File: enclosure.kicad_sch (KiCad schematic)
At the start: 17 parts, among them J101 Conn_01x06_Socket, J102 Conn_01x02_Socket

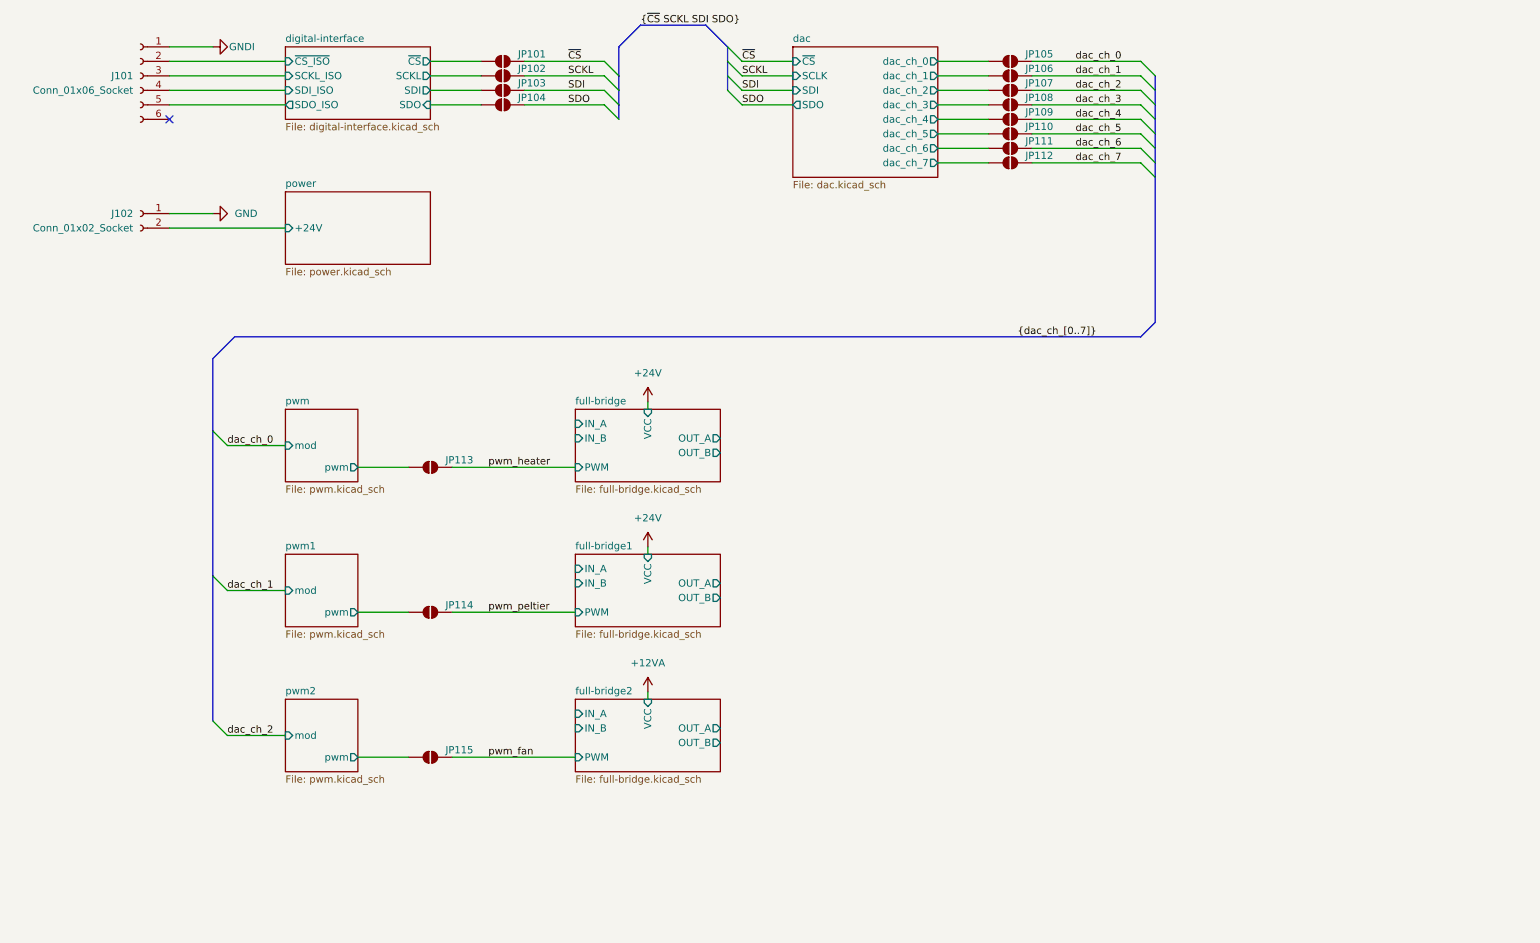
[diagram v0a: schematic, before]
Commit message: add enclosure output connectors
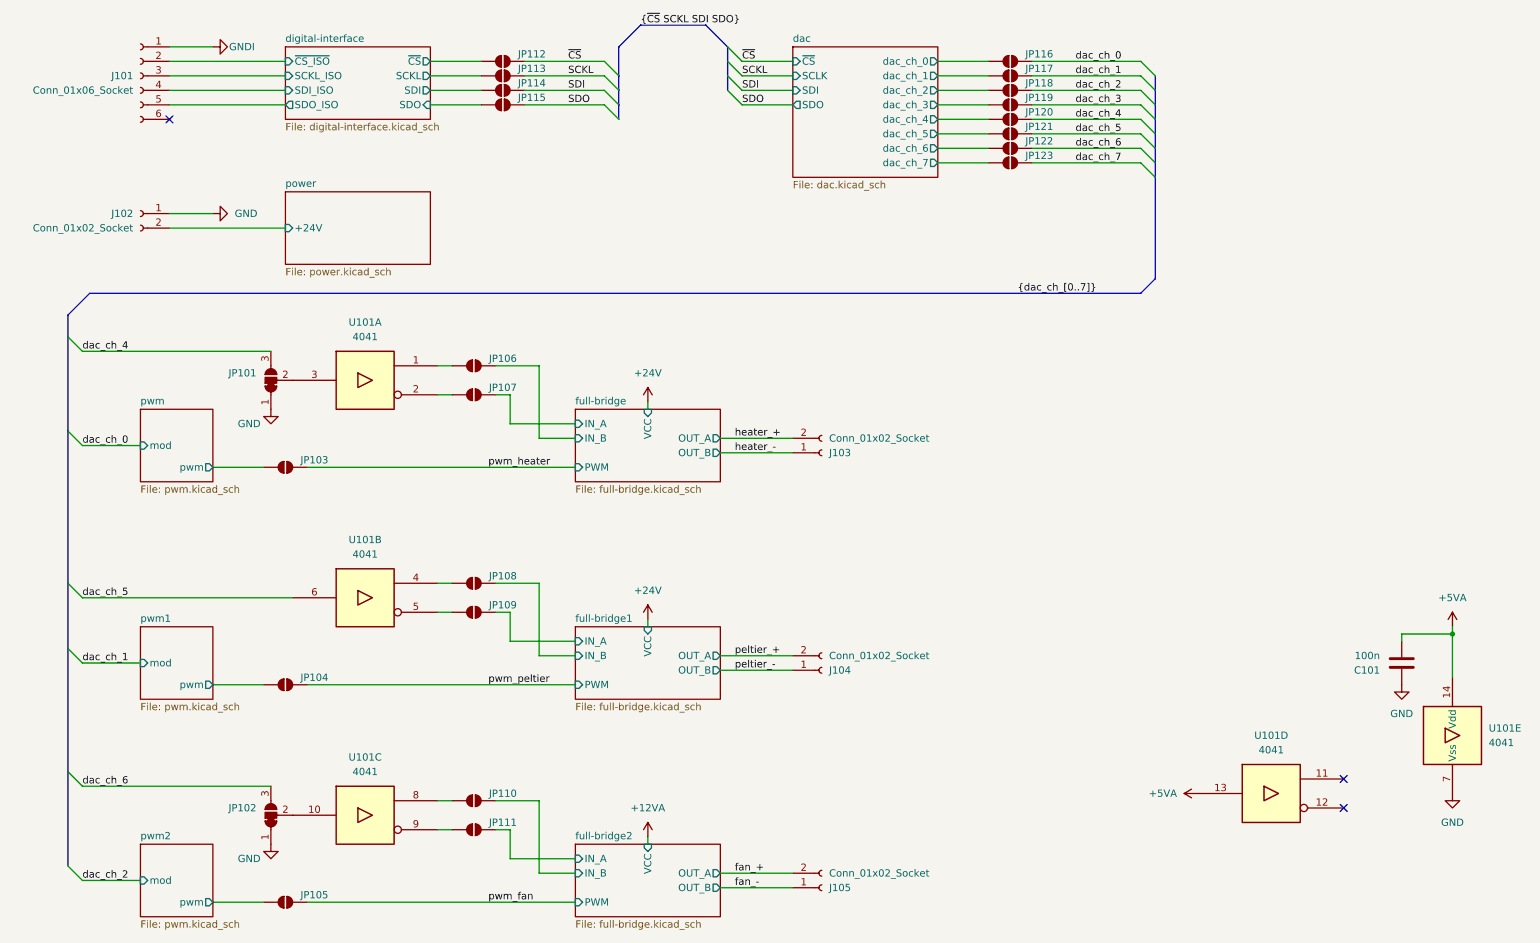
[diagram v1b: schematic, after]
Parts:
- added C101: 100n, pss:C_0805_2012Metric_Pad1.18x1.45mm_HandSolder, symbol enclosure:C
- added J103, J104, J105: Conn_01x02_Socket, pss:PhoenixContact_TDPT_2,5_2-SP-5,08_1x02_P5.08mm_Horizontal, symbol enclosure:Conn_01x02_Socket
- added JP101, JP102: SolderJumper_3_Bridged12, pss:SolderJumper-3_P1.3mm_Bridged12-Soldermask-Paste_RoundedPad1.0x1.5mm, symbol enclosure:SolderJumper_3_Bridged12
- added JP106, JP107, JP108, JP109, JP110, JP111: SolderJumper_2_Open, pss:SolderJumper-2_P1.3mm_Open_RoundedPad1.0x1.5mm, symbol enclosure:SolderJumper_2_Open
- added U101: 4041, pss:SOIC-14_3.9x8.7mm_P1.27mm, symbol enclosure:4041
- renumbered JP113 to JP103, JP114 to JP104, JP115 to JP105, JP101 to JP112, JP102 to JP113, JP103 to JP114, JP104 to JP115, JP105 to JP116, JP106 to JP117, JP107 to JP118, JP108 to JP119, JP109 to JP120, JP110 to JP121, JP111 to JP122, JP112 to JP123
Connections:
- net GND: now also C101.1, JP101.1 (A), JP102.1 (A), U101.7 (Vss)
- net dac_ch_4: now also JP101.3 (B)
- net dac_ch_5: now also U101.6
- net dac_ch_6: now also JP102.3 (B)
- net full-bridge/IN_A: now also JP107.2 (B)
- net full-bridge/IN_B: now also JP106.2 (B)
- net full-bridge1/IN_A: now also JP109.2 (B)
- net full-bridge1/IN_B: now also JP108.2 (B)
- net full-bridge2/IN_A: now also JP111.2 (B)
- net full-bridge2/IN_B: now also JP110.2 (B)
- new net: JP109.1 (A), U101.5
- new net: JP102.2 (C), U101.10
- new net: JP110.1 (A), U101.8
- new net: JP111.1 (A), U101.9
- new net: JP108.1 (A), U101.4
- new net: JP106.1 (A), U101.1
- new net: JP107.1 (A), U101.2
- new net: JP101.2 (C), U101.3
- new net +5VA: C101.2, U101.13, U101.14 (Vdd)
- new net fan_+: J105.2 (Pin_2)
- new net fan_-: J105.1 (Pin_1)
- new net heater_+: J103.2 (Pin_2)
- new net heater_-: J103.1 (Pin_1)
- new net peltier_+: J104.2 (Pin_2)
- new net peltier_-: J104.1 (Pin_1)
- no-connect marks 1 -> 3
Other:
- moved on the sheet: JP103, JP104, JP105

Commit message: update datasheets and footprint references
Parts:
- C101: footprint pss:C_0805_2012Metric_Pad1.18x1.45mm_HandSolder -> enclosure:C_0805_2012Metric_Pad1.18x1.45mm_HandSolder
- J101: footprint pss:PhoenixContact_TDPT_2,5_6-SP-5,08_1x06_P5.08mm_Horizontal -> enclosure:PhoenixContact_TDPT_2,5_6-SP-5,08_1x06_P5.08mm_Horizontal
- J102, J103, J104, J105: footprint pss:PhoenixContact_TDPT_2,5_2-SP-5,08_1x02_P5.08mm_Horizontal -> enclosure:PhoenixContact_TDPT_2,5_2-SP-5,08_1x02_P5.08mm_Horizontal
- JP101, JP102: footprint pss:SolderJumper-3_P1.3mm_Bridged12-Soldermask-Paste_RoundedPad1.0x1.5mm -> enclosure:SolderJumper-3_P1.3mm_Bridged12-Soldermask-Paste_RoundedPad1.0x1.5mm
- JP103, JP104, JP105, JP106, JP107, JP108, JP109, JP110, JP111, JP112, JP113, JP114, JP115, JP116, JP117, JP118, JP119, JP120, JP121, JP122, JP123: footprint pss:SolderJumper-2_P1.3mm_Open_RoundedPad1.0x1.5mm -> enclosure:SolderJumper-2_P1.3mm_Open_RoundedPad1.0x1.5mm
- U101: footprint pss:SOIC-14_3.9x8.7mm_P1.27mm -> enclosure:SOIC-14_3.9x8.7mm_P1.27mm
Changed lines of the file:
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@@
 			)
 		)
-		(property "Footprint" "pss:SolderJumper-2_P1.3mm_Open_RoundedPad1.0x1.5mm"
+		(property "Footprint" "enclosure:SolderJumper-2_P1.3mm_Open_RoundedPad1.0x1.5mm"
 			(at 101.6 30.48 0)
 			(effects
@@
 			)
 		)
-		(property "Footprint" "pss:SolderJumper-2_P1.3mm_Open_RoundedPad1.0x1.5mm"
+		(property "Footprint" "enclosure:SolderJumper-2_P1.3mm_Open_RoundedPad1.0x1.5mm"
 			(at 96.52 124.46 0)
 			(effects
@@
 			)
 		)
-		(property "Footprint" "pss:PhoenixContact_TDPT_2,5_2-SP-5,08_1x02_P5.08mm_Horizontal"
+		(property "Footprint" "enclosure:PhoenixContact_TDPT_2,5_2-SP-5,08_1x02_P5.08mm_Horizontal"
 			(at 38.1 54.61 0)
 			(effects
@@
 			)
 		)
-		(property "Footprint" "pss:SolderJumper-2_P1.3mm_Open_RoundedPad1.0x1.5mm"
+		(property "Footprint" "enclosure:SolderJumper-2_P1.3mm_Open_RoundedPad1.0x1.5mm"
 			(at 190.5 27.94 0)
 			(effects
@@
 			)
 		)
-		(property "Footprint" "pss:PhoenixContact_TDPT_2,5_6-SP-5,08_1x06_P5.08mm_Horizontal"
+		(property "Footprint" "enclosure:PhoenixContact_TDPT_2,5_6-SP-5,08_1x06_P5.08mm_Horizontal"
 			(at 38.1 30.48 0)
 			(effects
@@
 			)
 		)
-		(property "Footprint" "pss:SolderJumper-2_P1.3mm_Open_RoundedPad1.0x1.5mm"
+		(property "Footprint" "enclosure:SolderJumper-2_P1.3mm_Open_RoundedPad1.0x1.5mm"
 			(at 190.5 45.72 0)
 			(effects
@@
 			)
 		)
-		(property "Footprint" "pss:SolderJumper-2_P1.3mm_Open_RoundedPad1.0x1.5mm"
+		(property "Footprint" "enclosure:SolderJumper-2_P1.3mm_Open_RoundedPad1.0x1.5mm"
 			(at 190.5 38.1 0)
 			(effects
@@
 			)
 		)
-		(property "Footprint" "pss:PhoenixContact_TDPT_2,5_2-SP-5,08_1x02_P5.08mm_Horizontal"
+		(property "Footprint" "enclosure:PhoenixContact_TDPT_2,5_2-SP-5,08_1x02_P5.08mm_Horizontal"
 			(at 157.48 172.72 0)
 			(effects
@@
 			)
 		)
-		(property "Footprint" "pss:SolderJumper-2_P1.3mm_Open_RoundedPad1.0x1.5mm"
+		(property "Footprint" "enclosure:SolderJumper-2_P1.3mm_Open_RoundedPad1.0x1.5mm"
 			(at 190.5 40.64 0)
 			(effects
@@
 			)
 		)
-		(property "Footprint" "pss:PhoenixContact_TDPT_2,5_2-SP-5,08_1x02_P5.08mm_Horizontal"
+		(property "Footprint" "enclosure:PhoenixContact_TDPT_2,5_2-SP-5,08_1x02_P5.08mm_Horizontal"
 			(at 157.48 134.62 0)
 			(effects
@@
 			)
 		)
-		(property "Footprint" "pss:SolderJumper-2_P1.3mm_Open_RoundedPad1.0x1.5mm"
+		(property "Footprint" "enclosure:SolderJumper-2_P1.3mm_Open_RoundedPad1.0x1.5mm"
 			(at 190.5 33.02 0)
 			(effects
@@
 			)
 		)
-		(property "Footprint" "pss:SOIC-14_3.9x8.7mm_P1.27mm"
+		(property "Footprint" "enclosure:SOIC-14_3.9x8.7mm_P1.27mm"
 			(at 77.47 160.02 0)
 			(effects
@@
 			)
 		)
-		(property "Footprint" "pss:SolderJumper-2_P1.3mm_Open_RoundedPad1.0x1.5mm"
+		(property "Footprint" "enclosure:SolderJumper-2_P1.3mm_Open_RoundedPad1.0x1.5mm"
 			(at 96.52 119.38 0)
 			(effects
@@
 			)
 		)
-		(property "Footprint" "pss:SolderJumper-3_P1.3mm_Bridged12-Soldermask-Paste_RoundedPad1.0x1.5mm"
+		(property "Footprint" "enclosure:SolderJumper-3_P1.3mm_Bridged12-Soldermask-Paste_RoundedPad1.0x1.5mm"
 			(at 60.96 160.02 0)
 			(effects
@@
 			)
 		)
-		(property "Footprint" "pss:C_0805_2012Metric_Pad1.18x1.45mm_HandSolder"
+		(property "Footprint" "enclosure:C_0805_2012Metric_Pad1.18x1.45mm_HandSolder"
 			(at 258.1148 129.54 0)
 			(effects
@@
 			)
 		)
-		(property "Footprint" "pss:SolderJumper-2_P1.3mm_Open_RoundedPad1.0x1.5mm"
+		(property "Footprint" "enclosure:SolderJumper-2_P1.3mm_Open_RoundedPad1.0x1.5mm"
 			(at 96.52 157.48 0)
 			(effects
@@
 			)
 		)
-		(property "Footprint" "pss:SolderJumper-2_P1.3mm_Open_RoundedPad1.0x1.5mm"
+		(property "Footprint" "enclosure:SolderJumper-2_P1.3mm_Open_RoundedPad1.0x1.5mm"
 			(at 101.6 35.56 0)
 			(effects
@@
 			)
 		)
-		(property "Footprint" "pss:PhoenixContact_TDPT_2,5_2-SP-5,08_1x02_P5.08mm_Horizontal"
+		(property "Footprint" "enclosure:PhoenixContact_TDPT_2,5_2-SP-5,08_1x02_P5.08mm_Horizontal"
 			(at 157.48 96.52 0)
 			(effects
@@
 			)
 		)
-		(property "Footprint" "pss:SolderJumper-2_P1.3mm_Open_RoundedPad1.0x1.5mm"
+		(property "Footprint" "enclosure:SolderJumper-2_P1.3mm_Open_RoundedPad1.0x1.5mm"
 			(at 63.5 175.26 0)
 			(effects
@@
 			)
 		)
-		(property "Footprint" "pss:SolderJumper-2_P1.3mm_Open_RoundedPad1.0x1.5mm"
+		(property "Footprint" "enclosure:SolderJumper-2_P1.3mm_Open_RoundedPad1.0x1.5mm"
 			(at 190.5 43.18 0)
 			(effects
@@
 			)
 		)
-		(property "Footprint" "pss:SolderJumper-2_P1.3mm_Open_RoundedPad1.0x1.5mm"
+		(property "Footprint" "enclosure:SolderJumper-2_P1.3mm_Open_RoundedPad1.0x1.5mm"
 			(at 101.6 27.94 0)
 			(effects
@@
 			)
 		)
-		(property "Footprint" "pss:SOIC-14_3.9x8.7mm_P1.27mm"
+		(property "Footprint" "enclosure:SOIC-14_3.9x8.7mm_P1.27mm"
 			(at 77.47 83.82 0)
 			(effects
@@
 			)
 		)
-		(property "Footprint" "pss:SolderJumper-2_P1.3mm_Open_RoundedPad1.0x1.5mm"
+		(property "Footprint" "enclosure:SolderJumper-2_P1.3mm_Open_RoundedPad1.0x1.5mm"
 			(at 96.52 81.28 0)
 			(effects
@@
 			)
 		)
-		(property "Footprint" "pss:SOIC-14_3.9x8.7mm_P1.27mm"
+		(property "Footprint" "enclosure:SOIC-14_3.9x8.7mm_P1.27mm"
 			(at 77.47 121.92 0)
 			(effects
@@
 			)
 		)
-		(property "Footprint" "pss:SolderJumper-2_P1.3mm_Open_RoundedPad1.0x1.5mm"
+		(property "Footprint" "enclosure:SolderJumper-2_P1.3mm_Open_RoundedPad1.0x1.5mm"
 			(at 190.5 35.56 0)
 			(effects
@@
 			)
 		)
-		(property "Footprint" "pss:SolderJumper-2_P1.3mm_Open_RoundedPad1.0x1.5mm"
+		(property "Footprint" "enclosure:SolderJumper-2_P1.3mm_Open_RoundedPad1.0x1.5mm"
 			(at 190.5 30.48 0)
 			(effects
@@
 			)
 		)
-		(property "Footprint" "pss:SOIC-14_3.9x8.7mm_P1.27mm"
+		(property "Footprint" "enclosure:SOIC-14_3.9x8.7mm_P1.27mm"
 			(at 267.97 146.05 0)
 			(effects
@@
 			)
 		)
-		(property "Footprint" "pss:SOIC-14_3.9x8.7mm_P1.27mm"
+		(property "Footprint" "enclosure:SOIC-14_3.9x8.7mm_P1.27mm"
 			(at 236.22 156.21 0)
 			(effects
@@
 			)
 		)
-		(property "Footprint" "pss:SolderJumper-2_P1.3mm_Open_RoundedPad1.0x1.5mm"
+		(property "Footprint" "enclosure:SolderJumper-2_P1.3mm_Open_RoundedPad1.0x1.5mm"
 			(at 63.5 99.06 0)
 			(effects
@@
 			)
 		)
-		(property "Footprint" "pss:SolderJumper-2_P1.3mm_Open_RoundedPad1.0x1.5mm"
+		(property "Footprint" "enclosure:SolderJumper-2_P1.3mm_Open_RoundedPad1.0x1.5mm"
 			(at 63.5 137.16 0)
 			(effects
@@
 			)
 		)
-		(property "Footprint" "pss:SolderJumper-2_P1.3mm_Open_RoundedPad1.0x1.5mm"
+		(property "Footprint" "enclosure:SolderJumper-2_P1.3mm_Open_RoundedPad1.0x1.5mm"
 			(at 101.6 33.02 0)
 			(effects
@@
 			)
 		)
-		(property "Footprint" "pss:SolderJumper-2_P1.3mm_Open_RoundedPad1.0x1.5mm"
+		(property "Footprint" "enclosure:SolderJumper-2_P1.3mm_Open_RoundedPad1.0x1.5mm"
 			(at 96.52 162.56 0)
 			(effects
@@
 			)
 		)
-		(property "Footprint" "pss:SolderJumper-3_P1.3mm_Bridged12-Soldermask-Paste_RoundedPad1.0x1.5mm"
+		(property "Footprint" "enclosure:SolderJumper-3_P1.3mm_Bridged12-Soldermask-Paste_RoundedPad1.0x1.5mm"
 			(at 60.96 83.82 0)
 			(effects
@@
 			)
 		)
-		(property "Footprint" "pss:SolderJumper-2_P1.3mm_Open_RoundedPad1.0x1.5mm"
+		(property "Footprint" "enclosure:SolderJumper-2_P1.3mm_Open_RoundedPad1.0x1.5mm"
 			(at 96.52 86.36 0)
 			(effects

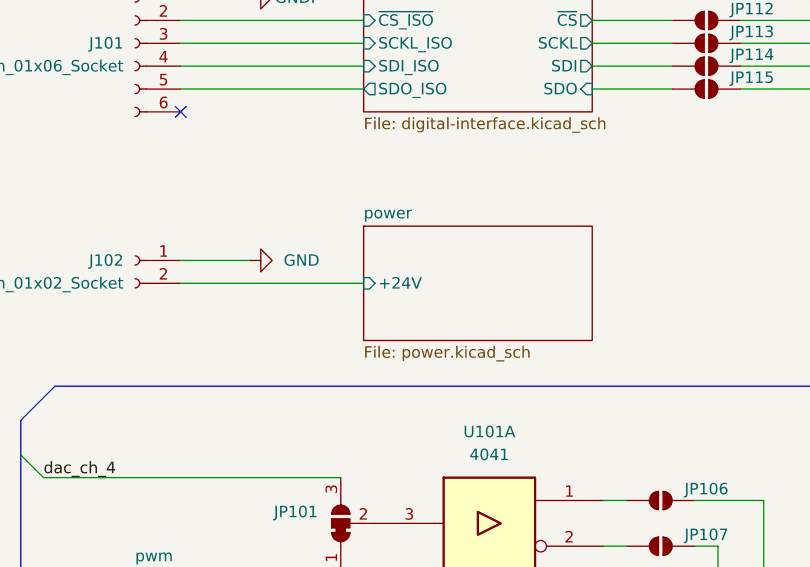
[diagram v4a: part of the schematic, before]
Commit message: fix netnaming collsion
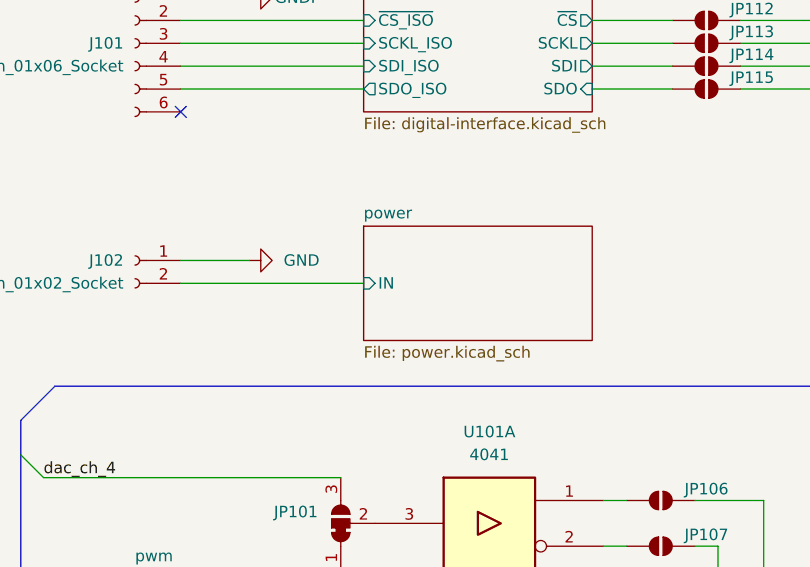
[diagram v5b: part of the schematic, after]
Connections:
- net power/+24V renamed power/IN
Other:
- sheet power ports: added IN; removed +24V
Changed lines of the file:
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@@
 			)
 		)
-		(pin "+24V" input
+		(pin "IN" input
 			(at 63.5 57.15 180)
 			(effects

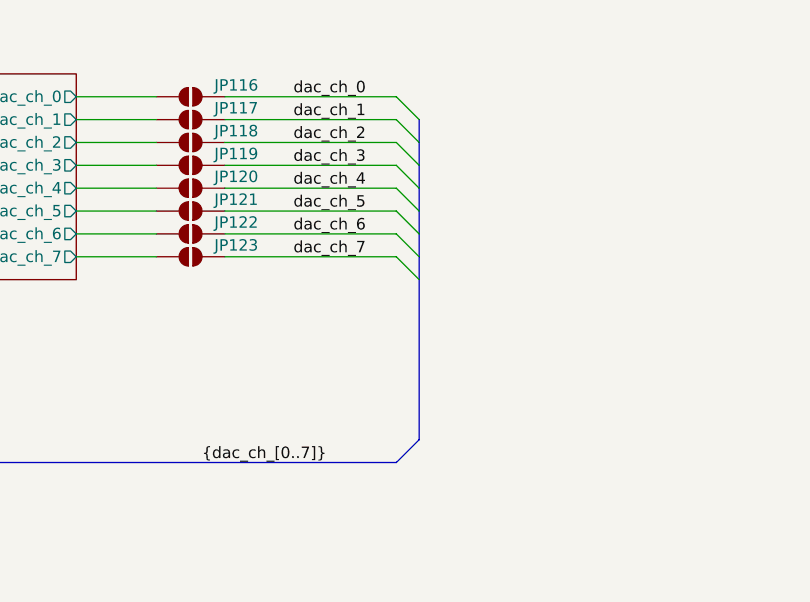
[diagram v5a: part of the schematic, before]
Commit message: fix erc errors
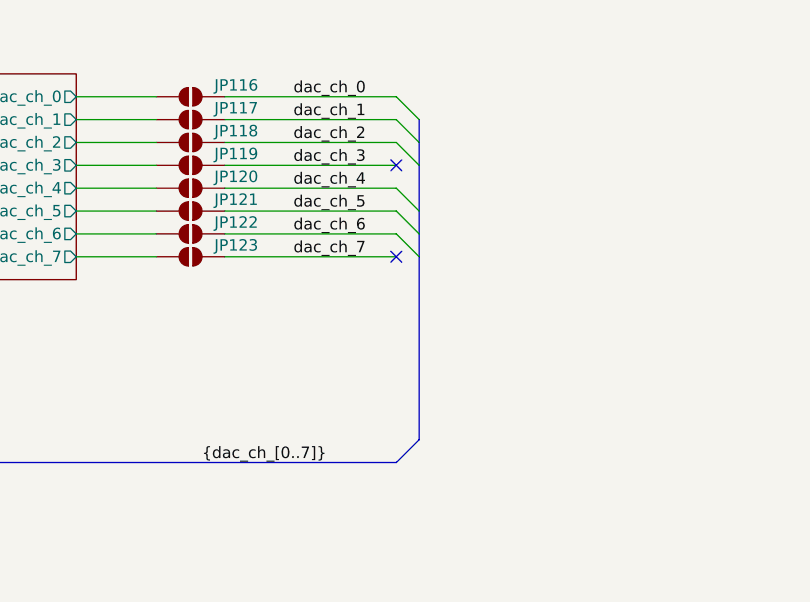
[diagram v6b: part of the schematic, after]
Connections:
- no-connect marks 3 -> 5
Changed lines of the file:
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@@
 	(title_block
 		(title "Power Supply Sink")
-		(date "2025-02-21")
-		(rev "1.1.1")
+		(date "2025-02-22")
+		(rev "1.1.2")
 		(company "Open Battery Tester")
 		(comment 1 "Overview")
@@
 	)
 	(no_connect
+		(at 213.36 35.56)
+	)
+	(no_connect
+		(at 213.36 45.72)
+	)
+	(no_connect
 		(at 248.92 158.75)
 	)
@@
 	)
 	(bus_entry
-		(at 213.36 35.56)
-		(size 2.54 2.54)
-		(stroke
-			(width 0)
-			(type default)
-		)
-	)
-	(bus_entry
 		(at 119.38 33.02)
 		(size 2.54 2.54)
@@
 	)
 	(bus_entry
-		(at 213.36 45.72)
-		(size 2.54 2.54)
-		(stroke
-			(width 0)
-			(type default)
-		)
-	)
-	(bus_entry
 		(at 25.4 76.2)
 		(size 2.54 2.54)
@@
 		)
 	)
-	(bus
-		(pts
-			(xy 215.9 35.56) (xy 215.9 38.1)
-		)
-		(stroke
-			(width 0)
-			(type default)
-		)
-	)
 	(wire
 		(pts
@@
 	(bus
 		(pts
-			(xy 215.9 38.1) (xy 215.9 40.64)
+			(xy 215.9 35.56) (xy 215.9 40.64)
 		)
 		(stroke
@@
 		)
 	)
-	(bus
-		(pts
-			(xy 215.9 48.26) (xy 215.9 66.04)
-		)
-		(stroke
-			(width 0)
-			(type default)
-		)
-	)
 	(wire
 		(pts
@@
 	(bus
 		(pts
-			(xy 215.9 45.72) (xy 215.9 48.26)
-		)
-		(stroke
+			(xy 215.9 45.72) (xy 215.9 66.04)
+		)
+		(stroke
